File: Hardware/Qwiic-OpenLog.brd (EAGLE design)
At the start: 38.1 x 38.1 mm, 65 parts, among them J1 MICRO-SD, J10 GATORGATOR_MINI, J2 GATORGATOR_MINI, J3 GATORGATOR_MINI, J4 GATORGATOR_MINI, J5 ISP, J6 GATORGATOR_MINI, J7 GATORGATOR_MINI, J8 GATORGATOR_MINI, J9 GATORGATOR_MINI, Q1 16MHZ, Q2 2.5A/30V/105mΩ, U1 RV-1805, U2 ATMEGA328P

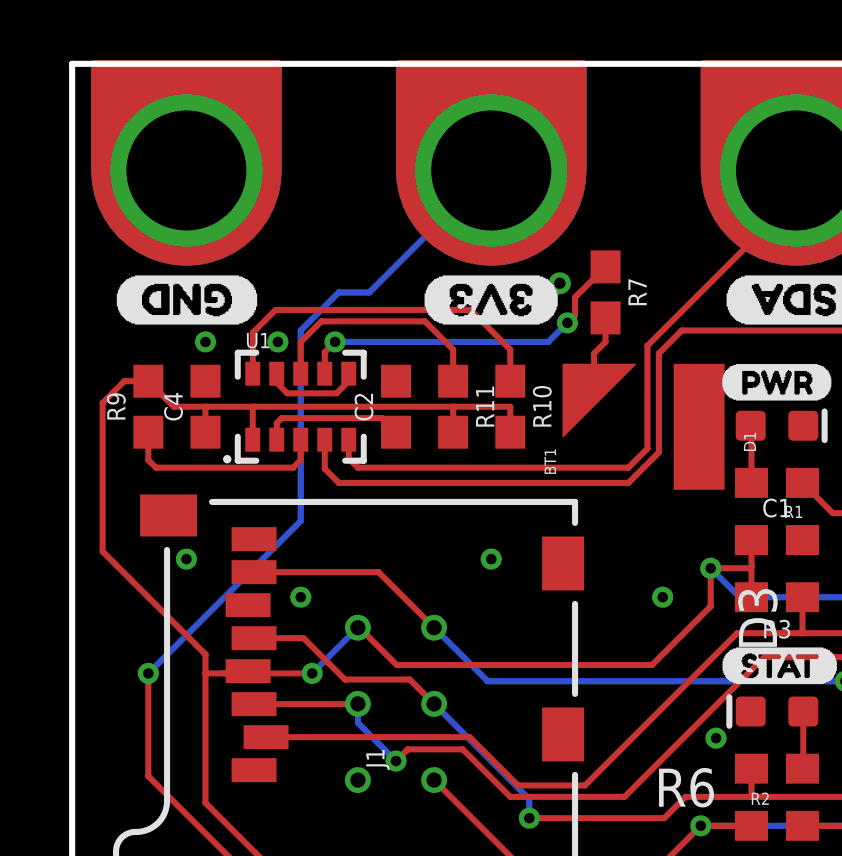
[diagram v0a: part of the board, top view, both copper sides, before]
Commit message: updating to RV-3028
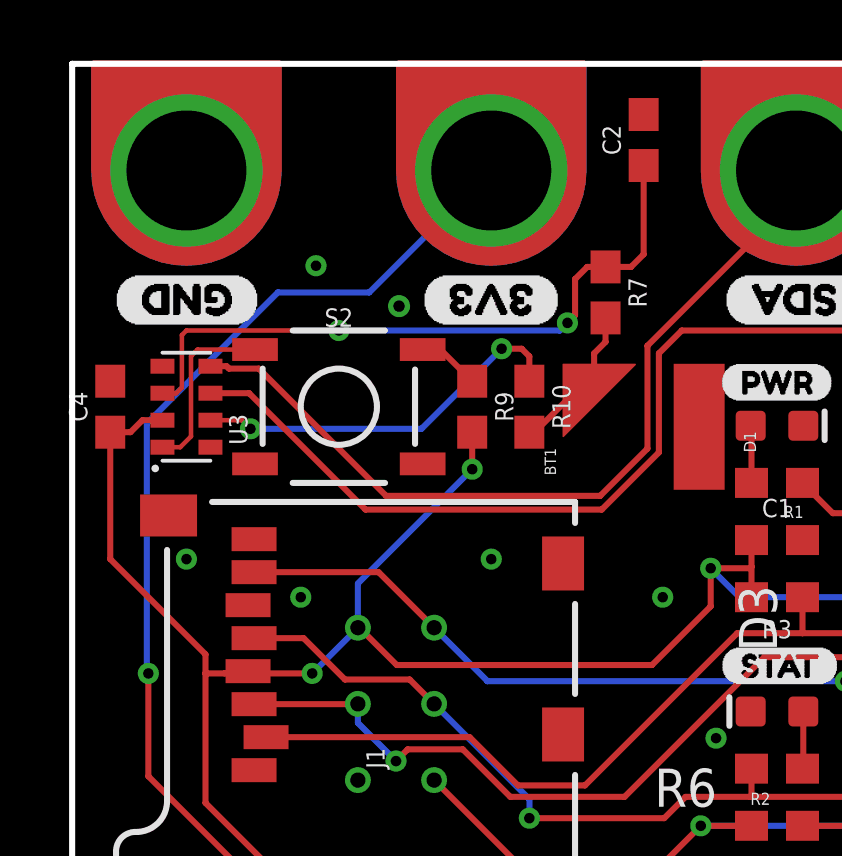
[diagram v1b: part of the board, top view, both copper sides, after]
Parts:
- removed R11: 10k, SparkFun-Resistors:0603
- removed U1: RV-1805, SparkFun-Clocks:RV-1805
- added S2: (no value), SparkFun-Switches:TACTILE_SWITCH_SMD_5.2MM
- added U3: RV-3028, SparkFun-Clocks:RV-3028
- C2: value 47pF -> 0.1uF
- C4: value 10nF -> 0.1uF
- R7: value 1k -> 470
- moved C2 12.1 mm to (19.1, 35.6)
- moved R9 10.8 mm to (13.3, 26.7), turned to 270 degrees
- moved C4 3.18 mm to (1.27, 26.7)
- moved R10 0.63 mm to (15.2, 26.7)
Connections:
- removed net !INT: R9.1, U1.3
- removed net N$10: C2.1, U1.2
- removed net PSW: R11.1, U1.8
- new net V_BATT: BT1.+, R10.2, R7.2
- net !RST: now also U3.2; no longer U1.10
- net 3.3V: now also U3.7; no longer R10.2, R11.2, U1.1
- net GND: now also S2.3, S2.4, U3.5; no longer U1.6, U1.9
- net N$8: now also R9.1, S2.1, S2.2, U3.8; no longer BT1.+, R7.2
- net SCL: now also U3.3; no longer U1.4
- net SDA: now also U3.4; no longer U1.5
- net VBACKUP: now also C2.1, U3.6; no longer U1.7
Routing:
- net VBACKUP: track 11.6 -> 22.7 mm
- net 3.3V: track 109.3 -> 100.3 mm, vias 3 -> 4
- net PSW: track 7.87 -> 0.00 mm
- net !INT: track 6.90 -> 0.00 mm
- net SDA: track 83.9 -> 90.0 mm
- net N$8: track 2.52 -> 8.09 mm
- net V_BATT: track 0.00 -> 4.97 mm
- net N$10: track 4.79 -> 0.00 mm
- net SCL: track 76.8 -> 81.4 mm
- net GND: track 3.26 -> 0.00 mm, vias 16 -> 15
- net N$5: track 44.0 -> 45.2 mm
- net !RST: track 11.9 -> 12.8 mm, vias 0 -> 2

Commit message: pre reds review changes
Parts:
- added U$23: (no value), buzzard_labels:GND0
- moved FID1 1.27 mm to (36.8, 29.2)
- moved FID4 1.27 mm to (36.8, 29.2)
- moved U$6 0.18 mm to (36.6, 30.2)
- moved U$13 0.13 mm to (21.7, 30.2)
- moved U$18 0.13 mm to (36.6, 7.87)
- moved U$16 0.13 mm to (26.5, 7.87)
- turned D1 to 180 degrees
- turned R1 to 0 degrees
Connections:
- removed net N$4: R1.1, U2.9
- net 3.3V: now also R1.1
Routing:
- net N$4: track 3.53 -> 0.00 mm
- net 3.3V: track 100.3 -> 102.2 mm
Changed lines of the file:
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@@
 <?xml version="1.0" encoding="utf-8"?>
 <!DOCTYPE eagle SYSTEM "eagle.dtd">
-<eagle version="9.1.0">
+<eagle version="9.1.2">
 <drawing>
 <settings>
@@
 <attribute name="VALUE" value="16MHZ" x="31.496" y="26.797" size="0.4064" layer="27"/>
 </element>
-<element name="R1" library="SparkFun-Resistors" package="0603" value="1k" x="23.495" y="24.13" smashed="yes" rot="R180">
-<attribute name="NAME" x="24.384" y="23.368" size="0.4064" layer="25" font="vector" rot="R180"/>
-<attribute name="PROD_ID" value="RES-07856" x="23.495" y="24.13" size="1.778" layer="27" rot="R180" display="off"/>
-<attribute name="VALUE" value="1k" x="25.654" y="24.384" size="0.4064" layer="27" font="vector" rot="R180"/>
-<attribute name="VALUE" value="1K" x="23.495" y="24.13" size="1.778" layer="27" rot="R180" display="off"/>
-</element>
-<element name="D1" library="SparkFun-LED" package="LED-0603" value="RED" x="23.495" y="26.035" smashed="yes">
-<attribute name="NAME" x="22.7965" y="25.146" size="0.4064" layer="25" rot="R90"/>
-<attribute name="PROD_ID" value="DIO-00819" x="23.495" y="26.035" size="1.778" layer="27" display="off"/>
-<attribute name="VALUE" x="21.971" y="26.289" size="0.4064" layer="27" rot="R180"/>
-<attribute name="VALUE" value="RED" x="23.495" y="26.035" size="1.778" layer="27" display="off"/>
+<element name="R1" library="SparkFun-Resistors" package="0603" value="1k" x="23.495" y="24.13" smashed="yes">
+<attribute name="NAME" x="22.606" y="24.892" size="0.4064" layer="25" font="vector"/>
+<attribute name="PROD_ID" value="RES-07856" x="23.495" y="24.13" size="1.778" layer="27" display="off"/>
+<attribute name="VALUE" value="1k" x="21.336" y="23.876" size="0.4064" layer="27" font="vector"/>
+<attribute name="VALUE" value="1K" x="23.495" y="24.13" size="1.778" layer="27" display="off"/>
+</element>
+<element name="D1" library="SparkFun-LED" package="LED-0603" value="RED" x="23.495" y="26.035" smashed="yes" rot="R180">
+<attribute name="NAME" x="24.1935" y="26.924" size="0.4064" layer="25" rot="R270"/>
+<attribute name="PROD_ID" value="DIO-00819" x="23.495" y="26.035" size="1.778" layer="27" rot="R180" display="off"/>
+<attribute name="VALUE" x="25.019" y="25.781" size="0.4064" layer="27"/>
+<attribute name="VALUE" value="RED" x="23.495" y="26.035" size="1.778" layer="27" rot="R180" display="off"/>
 </element>
 <element name="FRAME1" library="SparkFun-Aesthetics" package="CREATIVE_COMMONS" value="FRAME-LETTER" x="-21.062121875" y="-15.24" smashed="yes">
@@
 <attribute name="REV" value="" x="-21.062121875" y="-15.24" size="1.778" layer="27" display="off"/>
 </element>
-<element name="FID1" library="SparkFun-Aesthetics" package="FIDUCIAL-MICRO" value="FIDUCIALUFIDUCIAL" x="36.83" y="30.48" smashed="yes"/>
+<element name="FID1" library="SparkFun-Aesthetics" package="FIDUCIAL-MICRO" value="FIDUCIALUFIDUCIAL" x="36.83" y="29.21" smashed="yes"/>
 <element name="FID2" library="SparkFun-Aesthetics" package="FIDUCIAL-MICRO" value="FIDUCIALUFIDUCIAL" x="1.016" y="6.985" smashed="yes"/>
 <element name="LOGO2" library="SparkFun-Aesthetics" package="OSHW-LOGO-MINI" value="OSHW-LOGOMINI" x="19.05" y="2.54" smashed="yes" rot="MR0"/>
 <element name="FID3" library="SparkFun-Aesthetics" package="FIDUCIAL-MICRO" value="FIDUCIALUFIDUCIAL" x="1.016" y="6.985" smashed="yes" rot="MR180"/>
-<element name="FID4" library="SparkFun-Aesthetics" package="FIDUCIAL-MICRO" value="FIDUCIALUFIDUCIAL" x="36.83" y="30.48" smashed="yes" rot="MR0"/>
+<element name="FID4" library="SparkFun-Aesthetics" package="FIDUCIAL-MICRO" value="FIDUCIALUFIDUCIAL" x="36.83" y="29.21" smashed="yes" rot="MR0"/>
 <element name="C1" library="SparkFun-Capacitors" package="0603" value="4.7uF" x="23.495" y="22.225" smashed="yes">
 <attribute name="NAME" x="23.495" y="22.987" size="0.6096" layer="25" font="vector" ratio="20" align="bottom-center"/>
@@
 <element name="U$4" library="buzzard_labels" package="SDA1" value="" x="21.844" y="7.874" smashed="yes"/>
 <element name="U$5" library="buzzard_labels" package="SCL2" value="" x="32.131" y="7.874" smashed="yes"/>
-<element name="U$6" library="buzzard_labels" package="SCL2" value="" x="36.449" y="30.099" smashed="yes" rot="R180"/>
+<element name="U$6" library="buzzard_labels" package="SCL2" value="" x="36.576" y="30.226" smashed="yes" rot="R180"/>
 <element name="U$7" library="buzzard_labels" package="SDA1" value="" x="26.416" y="30.226" smashed="yes" rot="R180"/>
 <element name="U$10" library="buzzard_labels" package="GND0" value="" x="6.2484" y="30.226" smashed="yes" rot="R180"/>
 <element name="U$11" library="buzzard_labels" package="GND0" value="" x="1.3716" y="30.226" smashed="yes" rot="MR180"/>
 <element name="U$12" library="buzzard_labels" package="3V33" value="" x="11.6332" y="30.226" smashed="yes" rot="MR180"/>
-<element name="U$13" library="buzzard_labels" package="SDA1" value="" x="21.844" y="30.226" smashed="yes" rot="MR180"/>
+<element name="U$13" library="buzzard_labels" package="SDA1" value="" x="21.717" y="30.226" smashed="yes" rot="MR180"/>
 <element name="U$14" library="buzzard_labels" package="SCL2" value="" x="32.131" y="30.226" smashed="yes" rot="MR180"/>
 <element name="U$15" library="buzzard_labels" package="3V33" value="" x="16.3068" y="7.874" smashed="yes" rot="MR0"/>
-<element name="U$16" library="buzzard_labels" package="SDA1" value="" x="26.416" y="7.874" smashed="yes" rot="MR0"/>
-<element name="U$18" library="buzzard_labels" package="SCL2" value="" x="36.449" y="7.874" smashed="yes" rot="MR0"/>
+<element name="U$16" library="buzzard_labels" package="SDA1" value="" x="26.543" y="7.874" smashed="yes" rot="MR0"/>
+<element name="U$18" library="buzzard_labels" package="SCL2" value="" x="36.576" y="7.874" smashed="yes" rot="MR0"/>
 <element name="D2" library="SparkFun-DiscreteSemi" package="SOD-323" value="3.6V" x="10.287" y="6.985" smashed="yes" rot="R270">
 <attribute name="NAME" x="11.049" y="6.985" size="0.6096" layer="25" font="vector" ratio="20" rot="R270" align="bottom-center"/>
@@
 <attribute name="PROD_ID" value="SWCH-14139" x="8.89" y="26.67" size="1.778" layer="27" display="off"/>
 </element>
+<element name="U$23" library="buzzard_labels" package="GND0" value="" x="6.2484" y="7.874" smashed="yes" rot="MR0"/>
 </elements>
 <signals>
@@
 <contactref element="R1" pad="2"/>
 <contactref element="D1" pad="A"/>
-<wire x1="22.645" y1="24.13" x2="22.645" y2="26.008" width="0.2032" layer="1"/>
-<wire x1="22.645" y1="26.008" x2="22.618" y2="26.035" width="0.2032" layer="1"/>
+<wire x1="24.372" y1="26.035" x2="24.345" y2="26.008" width="0.2032" layer="1"/>
+<wire x1="24.345" y1="26.008" x2="24.345" y2="24.13" width="0.2032" layer="1"/>
 </signal>
 <signal name="CS">
@@
 <wire x1="17.0942" y1="14.0462" x2="22.168" y2="19.12" width="0.2032" layer="1"/>
 <wire x1="24.345" y1="20.32" x2="24.345" y2="19.12" width="0.2032" layer="1"/>
-</signal>
-<signal name="N$4">
-<contactref element="R1" pad="1"/>
-<contactref element="U2" pad="9"/>
-<wire x1="24.345" y1="24.13" x2="25.355" y2="23.12" width="0.2032" layer="1"/>
-<wire x1="25.355" y1="23.12" x2="27.4574" y2="23.12" width="0.2032" layer="1"/>
 </signal>
 <signal name="3.3V">
@@
 <wire x1="19.3294" y1="18.0594" x2="21.2852" y2="20.0152" width="0.2032" layer="1"/>
 <via x="31.35" y="20.32" extent="1-16" drill="0.35"/>
-<wire x1="4.445" y1="17.78" x2="5.08" y2="17.78" width="0.2032" layer="1"/>
-<wire x1="5.08" y1="17.78" x2="5.939" y2="17.78" width="0.2032" layer="1"/>
+<wire x1="4.445" y1="17.78" x2="5.939" y2="17.78" width="0.2032" layer="1"/>
 <wire x1="31.35" y1="21.825" x2="31.35" y2="20.32" width="0.2032" layer="1"/>
 <via x="21.2852" y="21.2852" extent="1-16" drill="0.35"/>
@@
 <wire x1="25.273" y1="10.668" x2="26.035" y2="11.43" width="0.2032" layer="1"/>
 <wire x1="26.035" y1="11.43" x2="26.035" y2="12.7" width="0.2032" layer="1"/>
-<wire x1="34.075" y1="13.97" x2="34.075" y2="13.589" width="0.2032" layer="1"/>
-<wire x1="34.075" y1="13.589" x2="34.075" y2="12.954" width="0.2032" layer="1"/>
+<wire x1="34.075" y1="13.97" x2="34.075" y2="12.954" width="0.2032" layer="1"/>
 <wire x1="34.075" y1="12.954" x2="34.075" y2="12.065" width="0.2032" layer="1"/>
 <wire x1="31.35" y1="12.935" x2="31.115" y2="12.7" width="0.2032" layer="1"/>
@@
 <wire x1="13.335" y1="24.5872" x2="9.525" y2="20.7772" width="0.2032" layer="16"/>
 <wire x1="9.525" y1="20.7772" x2="9.525" y2="19.304" width="0.2032" layer="16"/>
+<contactref element="R1" pad="1"/>
+<wire x1="22.645" y1="22.225" x2="22.645" y2="24.13" width="0.2032" layer="1"/>
 </signal>
 <signal name="SCL">

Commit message: engineer run of checklist
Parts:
- added U$24: (no value), buzzard_labels (17):GATOR#LOG0
- U$19: device buzzard_labels (4):GATOR#LOG3 -> buzzard_labels (18):TIMESTAMP0
- moved D5 30.5 mm to (29.2, 34.3), turned to 90 degrees
- moved U$19 20.2 mm to (8.76, 29.1), flipped to the top, turned to 90 degrees
- moved Q2 11.3 mm to (19.1, 6.35), turned to 180 degrees
- moved R8 10.2 mm to (19.1, 2.54)
- moved D4 10.2 mm to (29.2, 3.81)
- moved D2 8.97 mm to (19.1, 8.89), turned to 0 degrees
- moved LOGO1 7.62 mm to (19.1, 16.5)
- moved R7 1.80 mm to (19.1, 31.8)
- moved LOGO4 1.27 mm to (19.1, 18.3)
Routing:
- net 3.3V: track 102.2 -> 110.1 mm
- net SDA: track 90.0 -> 86.4 mm
- net N$5: track 45.2 -> 48.5 mm
- net N$8: track 8.09 -> 11.3 mm, vias 0 -> 2
- net N$6: track 3.01 -> 5.98 mm
- net SCL: track 81.4 -> 78.9 mm
- net V_BATT: track 4.97 -> 7.28 mm
- net VBACKUP: track 22.7 -> 21.9 mm
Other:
- board text added: "v10"
- board text removed: "v01"
